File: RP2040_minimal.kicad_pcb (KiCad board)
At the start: 2 copper layers, 52 x 51 mm, 34 parts, among them J1 USB_B_Micro, J2 Conn_01x02, J3 Conn_02x18_Odd_Even, J4 Conn_02x18_Odd_Even, U1 NCP1117-3.3_SOT223, U2 W25Q128JVS, U3 RP2040, Y1 ABLS-12.000MHZ-B4-T

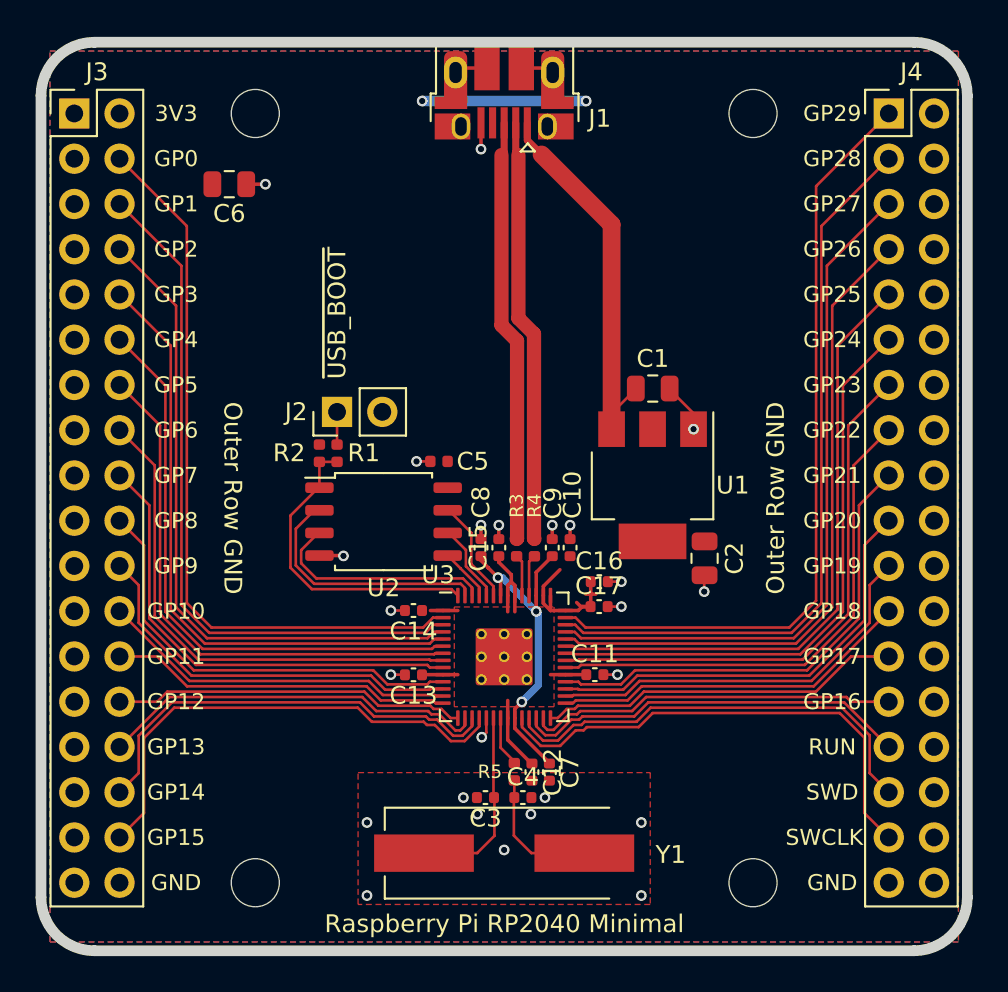
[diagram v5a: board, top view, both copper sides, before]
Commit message: Replaced USB Micro A receptacle with USB C Added 5k1 resistors for UFP identification Added jumpers connecting CC1 to GPIO21, CC2 to GPIO22, SBU2 to GPIO0,   and SBU2 to GPIO1. Added jumper for VBUS
Updated README.md
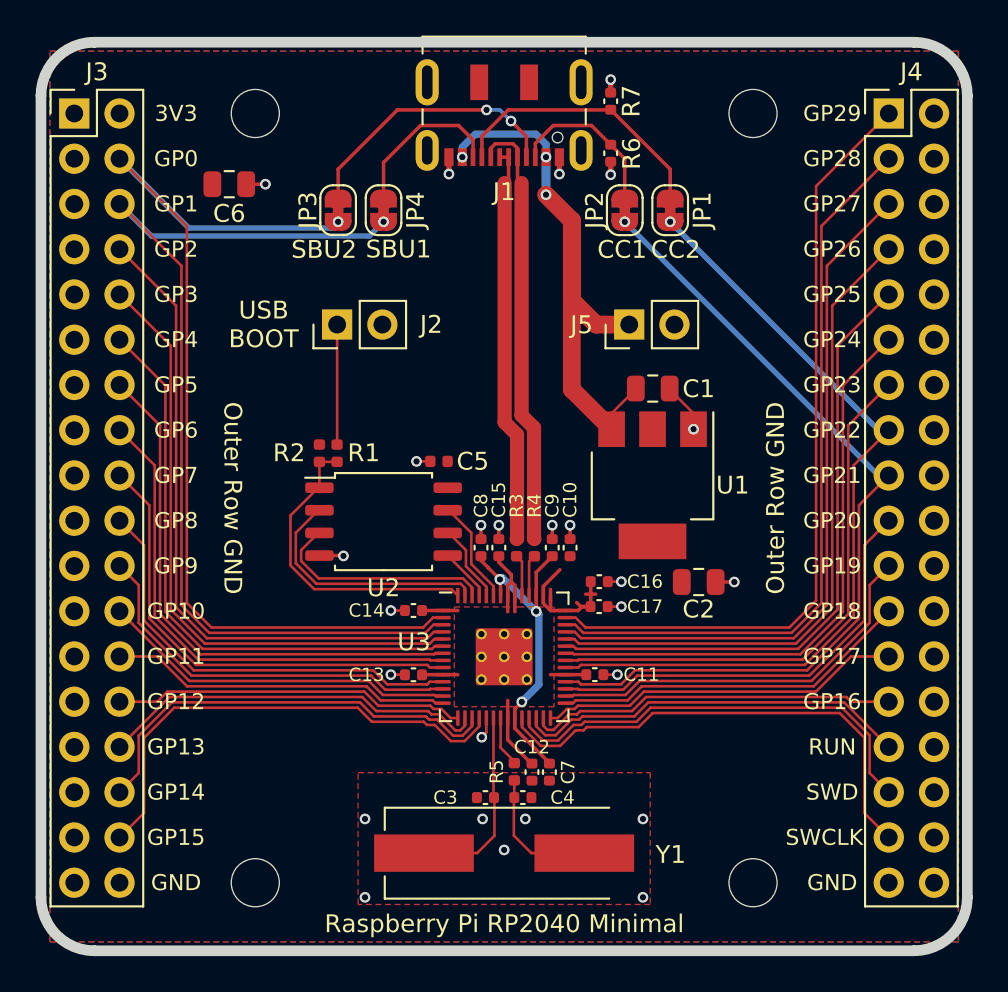
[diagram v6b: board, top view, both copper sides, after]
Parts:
- added J5: Conn_01x02, Connector_PinHeader_2.54mm:PinHeader_1x02_P2.54mm_Vertical, F.Cu at (107.0, 85.8)
- added JP1: SolderJumper_2_Bridged, Jumper:SolderJumper-2_P1.3mm_Bridged_RoundedPad1.0x1.5mm, F.Cu at (109.3, 79.4)
- added JP2: SolderJumper_2_Bridged, Jumper:SolderJumper-2_P1.3mm_Bridged_RoundedPad1.0x1.5mm, F.Cu at (106.8, 79.4)
- added JP3: SolderJumper_2_Bridged, Jumper:SolderJumper-2_P1.3mm_Bridged_RoundedPad1.0x1.5mm, F.Cu at (90.7, 79.4)
- added JP4: SolderJumper_2_Bridged, Jumper:SolderJumper-2_P1.3mm_Bridged_RoundedPad1.0x1.5mm, F.Cu at (93.2, 79.4)
- added R6: 5k1, Capacitor_SMD:C_0402_1005Metric, F.Cu at (106.0, 76.2)
- added R7: 5k1, Capacitor_SMD:C_0402_1005Metric, F.Cu at (106.0, 73.3)
- J1: value USB_B_Micro -> USB_C_Receptacle_USB2.0; footprint RP2040_minimal:USB_Micro-B_Amphenol_10103594-0001LF_Horizontal_modified -> Connector_USB:USB_C_Receptacle_JAE_DX07S016JA1R1500
- moved J2 4.90 mm to (90.6, 85.8)
- moved J1 1.70 mm to (100.0, 73.4)
- moved C2 1.37 mm to (110.9, 100.3), turned to 0 degrees
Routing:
- net /GPIO21: track 26.8 -> 47.5 mm, vias 0 -> 1
- net /GPIO22: track 28.6 -> 45.7 mm, vias 0 -> 1
- net /GPIO1: track 39.5 -> 55.4 mm, vias 0 -> 1
- net /CC2: track 0.00 -> 15.4 mm
- net /SBU2: track 0.00 -> 15.4 mm, vias 0 -> 2
- net /GPIO0: track 41.7 -> 55.7 mm, vias 0 -> 1
- net VBUS: track 22.0 -> 34.4 mm, vias 0 -> 3
- net /CC1: track 0.00 -> 9.22 mm
- net /SBU1: track 0.00 -> 9.21 mm
- net +3V3: track 33.0 -> 24.3 mm, vias 2 -> 0
- net /~{USB_BOOT}: track 1.83 -> 6.74 mm
- net GND: track 20.3 -> 18.6 mm, vias 25 -> 26
- net /USB_D+: track 23.8 -> 22.3 mm
- net /USB_D-: track 23.8 -> 24.5 mm
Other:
- board text added: "CC1"
- board text added: "CC2"
- board text added: "SBU1"
- board text added: "SBU2"
- board text added: "USB BOOT"
- board text removed: "~{USB_BOOT}"

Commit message: Really updated README.md this time.
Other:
- board text added: "VBUS"
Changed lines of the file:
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@@
+    (effects (font (size 1 1) (thickness 0.15)))
+  )
+  (gr_text "VBUS" (at 113.4 85.85) (layer "F.SilkS")
     (effects (font (size 1 1) (thickness 0.15)))
   )
